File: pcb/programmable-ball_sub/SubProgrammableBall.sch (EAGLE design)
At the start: 9 parts, among them CON1 B4B-ZR-SM4-TF, U2 LSM6DS0TR

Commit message: 軽微な修正
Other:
- moved on the sheet: C1, C2, FB1, R1, R2, R3, R4, U2

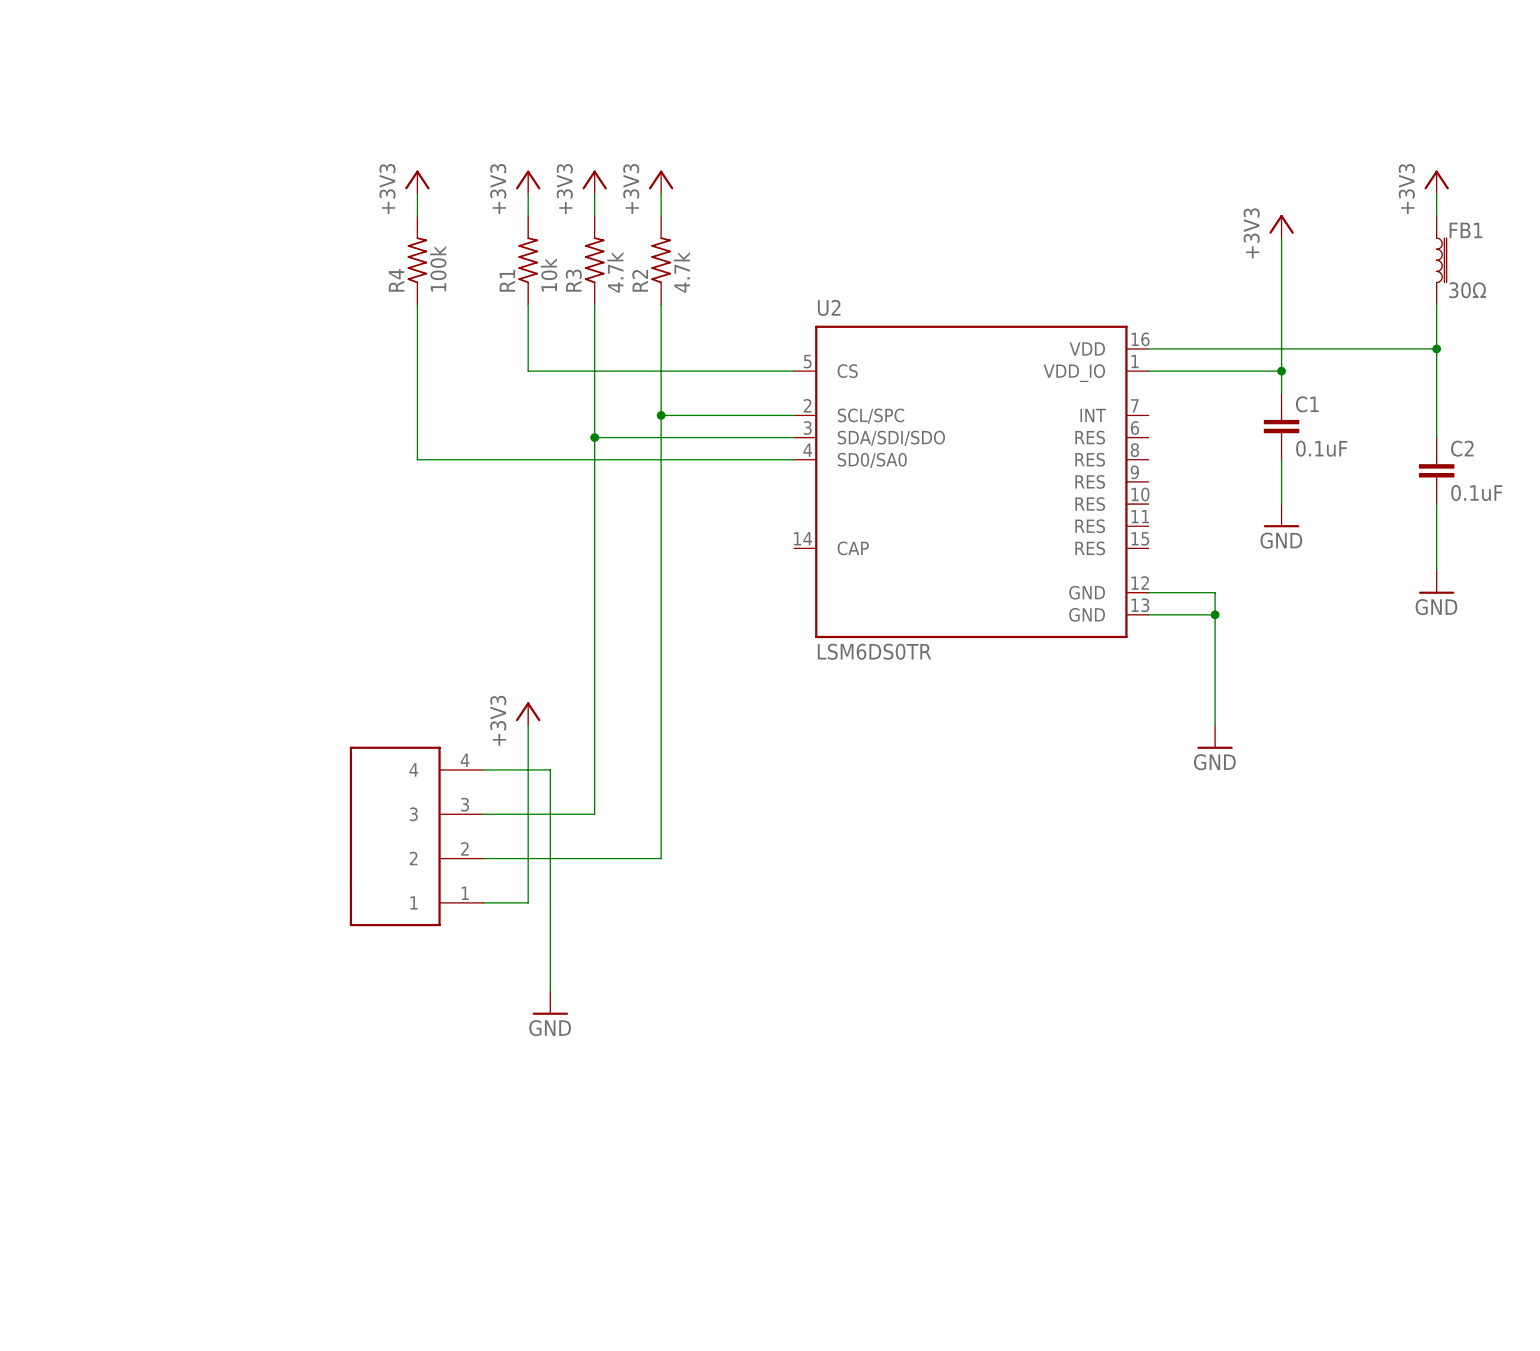
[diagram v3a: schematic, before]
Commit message: 加速度センサのfoot print間違い修正
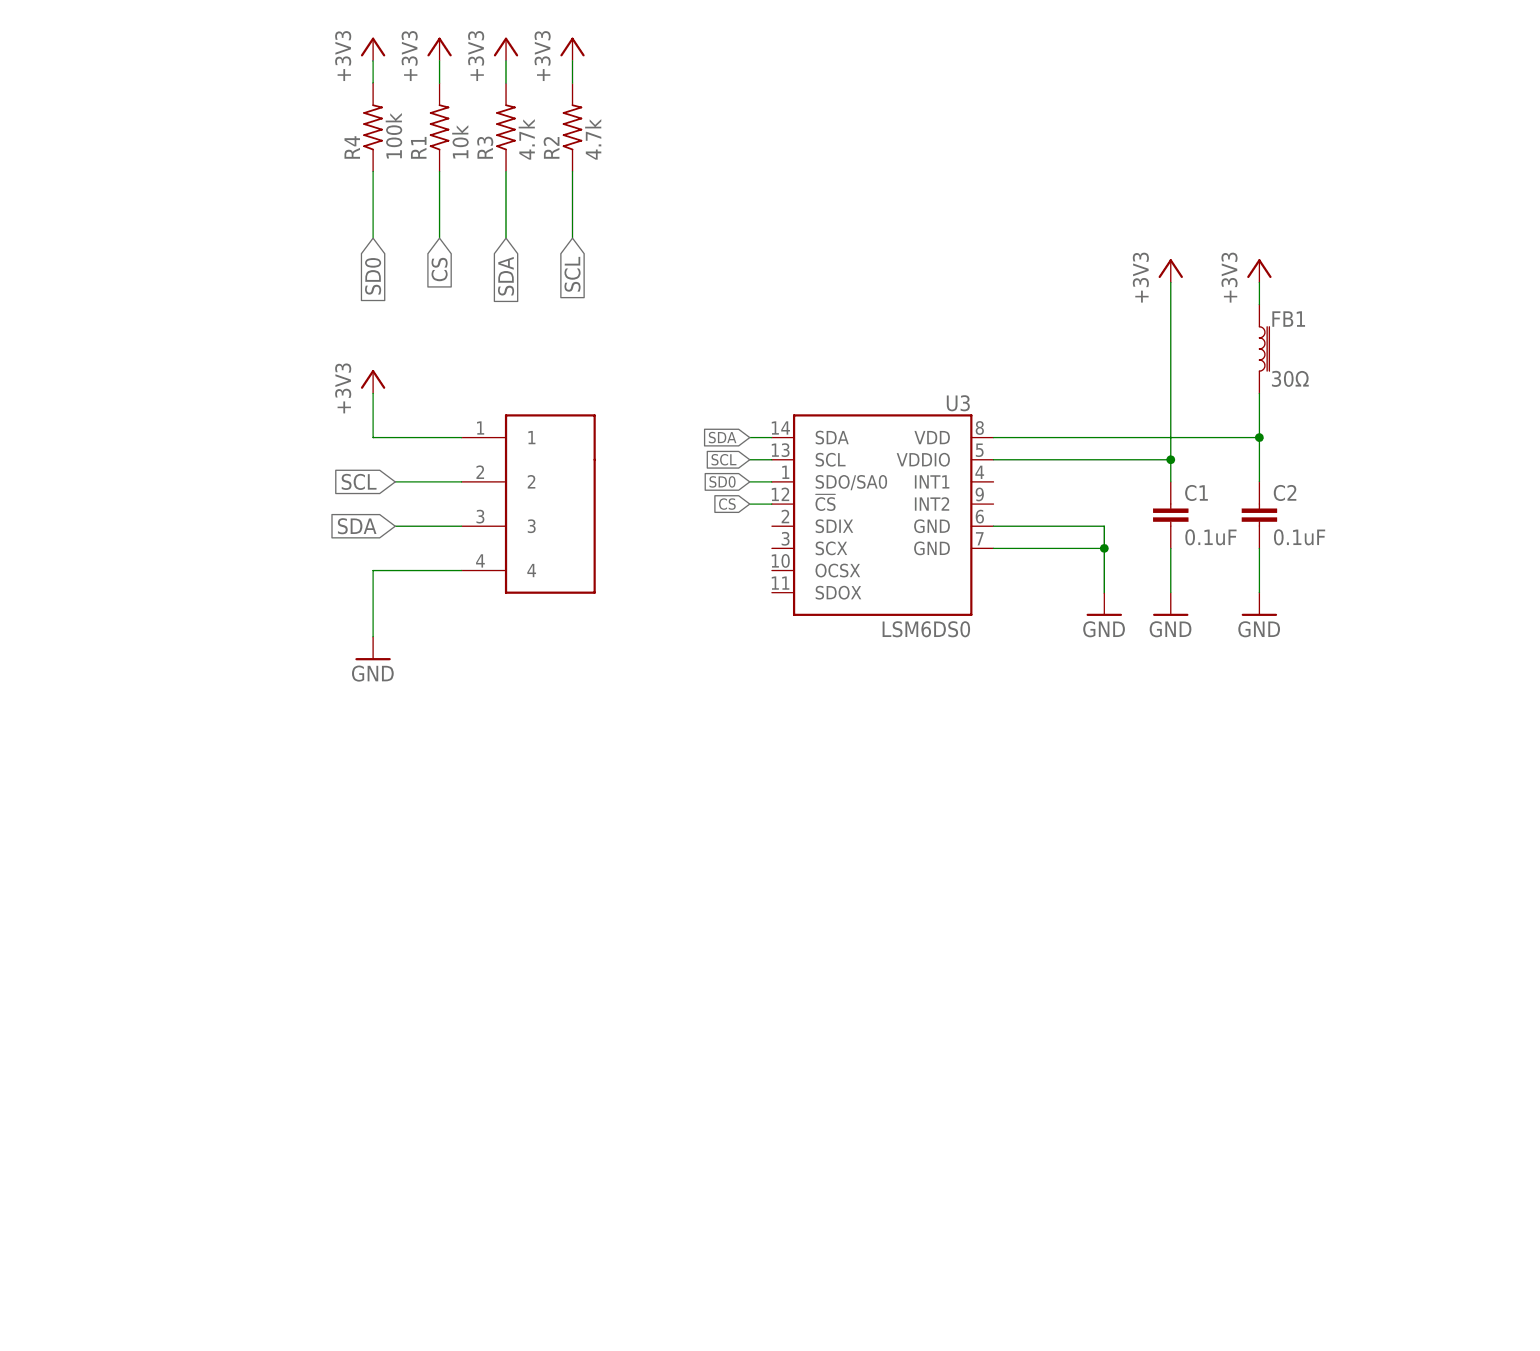
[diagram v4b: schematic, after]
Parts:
- removed U2: LSM6DS0TR, SubProgrammableBall:LSM6DS0TR
- added U3: LSM6DS0, temp:LSM6DS0
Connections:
- removed net N$2: R1.1, U2.CS
- removed net N$3: CON1.3, R3.1, U2.SDA/SDI/SDO
- removed net N$5: R4.1, U2.SD0/SA0
- new net CS: R1.1, U3.!CS!
- new net SD0: R4.1, U3.SDO/SA0
- new net SDA: CON1.3, R3.1, U3.SDA
- net +3V3: now also U3.VDDIO; no longer U2.VDD_IO
- net GND: now also U3.GND@6, U3.GND@7; no longer U2.GND, U2.GND@1
- net N$1: now also U3.VDD; no longer U2.VDD
- net SCL: now also U3.SCL; no longer U2.SCL/SPC
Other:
- moved on the sheet: C1, C2, FB1, R1, R2, R3, R4
